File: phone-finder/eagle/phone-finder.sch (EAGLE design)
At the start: 45 parts, among them J1 MICRO USB, J2 PHONE-JACK, K1 RELAY, Q1 12Mhz, Q2 2N2222, Q3 2N2222, T1 DTA114EET1G (2x10K), U1 AP2114H-3.3TRG1, U2 NUF2042XV6T1G, U3 LPC11U35FHI33/501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

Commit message: Layout work in progress.
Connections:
- removed net N$20: K12.S2, R12.2
- new net N$15: K12.S1, R12.2
- net N$11: now also K12.S2; no longer K12.S1
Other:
- moved on the sheet: U1
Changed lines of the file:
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@@
 <attribute name="PART" x="355.981" y="70.358" size="1.778" layer="95"/>
 </instance>
-<instance part="K1" gate="2" x="360.68" y="119.38" smashed="yes" rot="R270">
-<attribute name="PART" x="362.839" y="114.935" size="1.778" layer="95"/>
+<instance part="K1" gate="2" x="360.68" y="119.38" smashed="yes" rot="MR270">
+<attribute name="PART" x="358.521" y="114.935" size="1.778" layer="95" rot="MR0"/>
 </instance>
 <instance part="+5V3" gate="G$1" x="350.52" y="83.82" rot="MR0"/>
@@
 </segment>
 </net>
-<net name="N$20" class="0">
-<segment>
-<pinref part="R12" gate="G$1" pin="2"/>
-<pinref part="K1" gate="2" pin="S2"/>
-<wire x1="350.52" y1="119.38" x2="353.06" y2="119.38" width="0.1524" layer="91"/>
-</segment>
-</net>
 <net name="N$17" class="0">
 <segment>
@@
 <net name="N$11" class="0">
 <segment>
-<pinref part="K1" gate="2" pin="S1"/>
-<wire x1="368.3" y1="119.38" x2="370.84" y2="119.38" width="0.1524" layer="91"/>
 <wire x1="370.84" y1="119.38" x2="370.84" y2="114.3" width="0.1524" layer="91"/>
 <pinref part="J2" gate="G$1" pin="4"/>
 <wire x1="370.84" y1="114.3" x2="375.92" y2="114.3" width="0.1524" layer="91"/>
+<pinref part="K1" gate="2" pin="S2"/>
+<wire x1="368.3" y1="119.38" x2="370.84" y2="119.38" width="0.1524" layer="91"/>
 </segment>
 </net>
@@
 </segment>
 </net>
+<net name="N$15" class="0">
+<segment>
+<pinref part="R12" gate="G$1" pin="2"/>
+<pinref part="K1" gate="2" pin="S1"/>
+<wire x1="350.52" y1="119.38" x2="353.06" y2="119.38" width="0.1524" layer="91"/>
+</segment>
+</net>

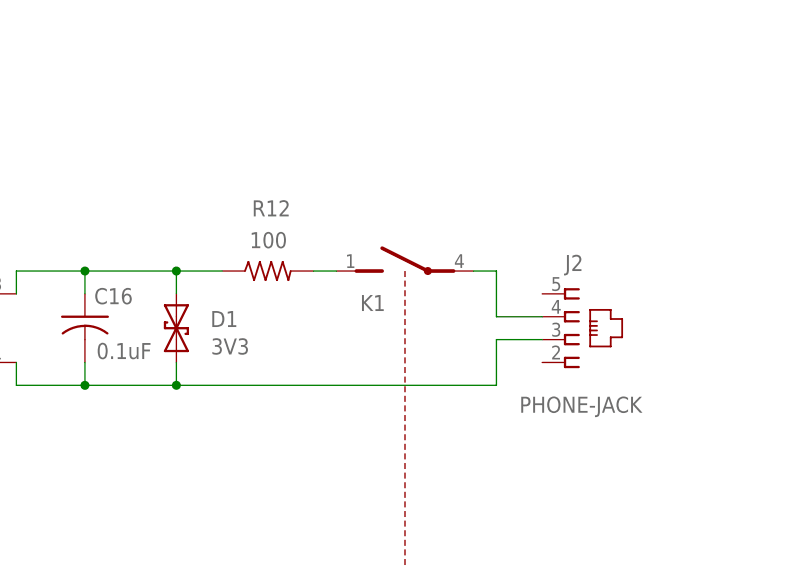
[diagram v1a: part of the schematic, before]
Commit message: Critical net routing done.
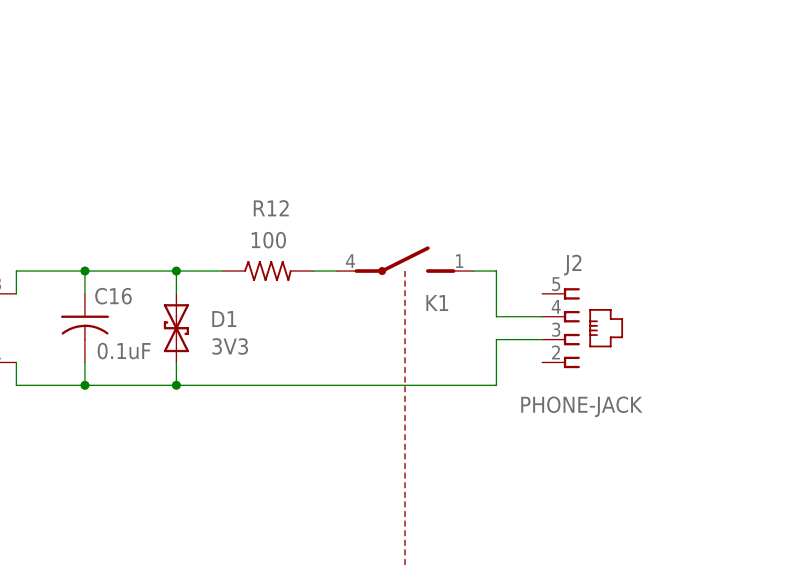
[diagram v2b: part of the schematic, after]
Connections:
- net N$11: now also K12.S1; no longer K12.S2
- net N$15: now also K12.S2; no longer K12.S1
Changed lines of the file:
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@@
 <attribute name="PART" x="355.981" y="70.358" size="1.778" layer="95"/>
 </instance>
-<instance part="K1" gate="2" x="360.68" y="119.38" smashed="yes" rot="MR270">
-<attribute name="PART" x="358.521" y="114.935" size="1.778" layer="95" rot="MR0"/>
+<instance part="K1" gate="2" x="360.68" y="119.38" smashed="yes" rot="R270">
+<attribute name="PART" x="362.839" y="114.935" size="1.778" layer="95"/>
 </instance>
 <instance part="+5V3" gate="G$1" x="350.52" y="83.82" rot="MR0"/>
@@
 <pinref part="J2" gate="G$1" pin="4"/>
 <wire x1="370.84" y1="114.3" x2="375.92" y2="114.3" width="0.1524" layer="91"/>
-<pinref part="K1" gate="2" pin="S2"/>
+<pinref part="K1" gate="2" pin="S1"/>
 <wire x1="368.3" y1="119.38" x2="370.84" y2="119.38" width="0.1524" layer="91"/>
 </segment>
@@
 <segment>
 <pinref part="R12" gate="G$1" pin="2"/>
-<pinref part="K1" gate="2" pin="S1"/>
+<pinref part="K1" gate="2" pin="S2"/>
 <wire x1="350.52" y1="119.38" x2="353.06" y2="119.38" width="0.1524" layer="91"/>
 </segment>

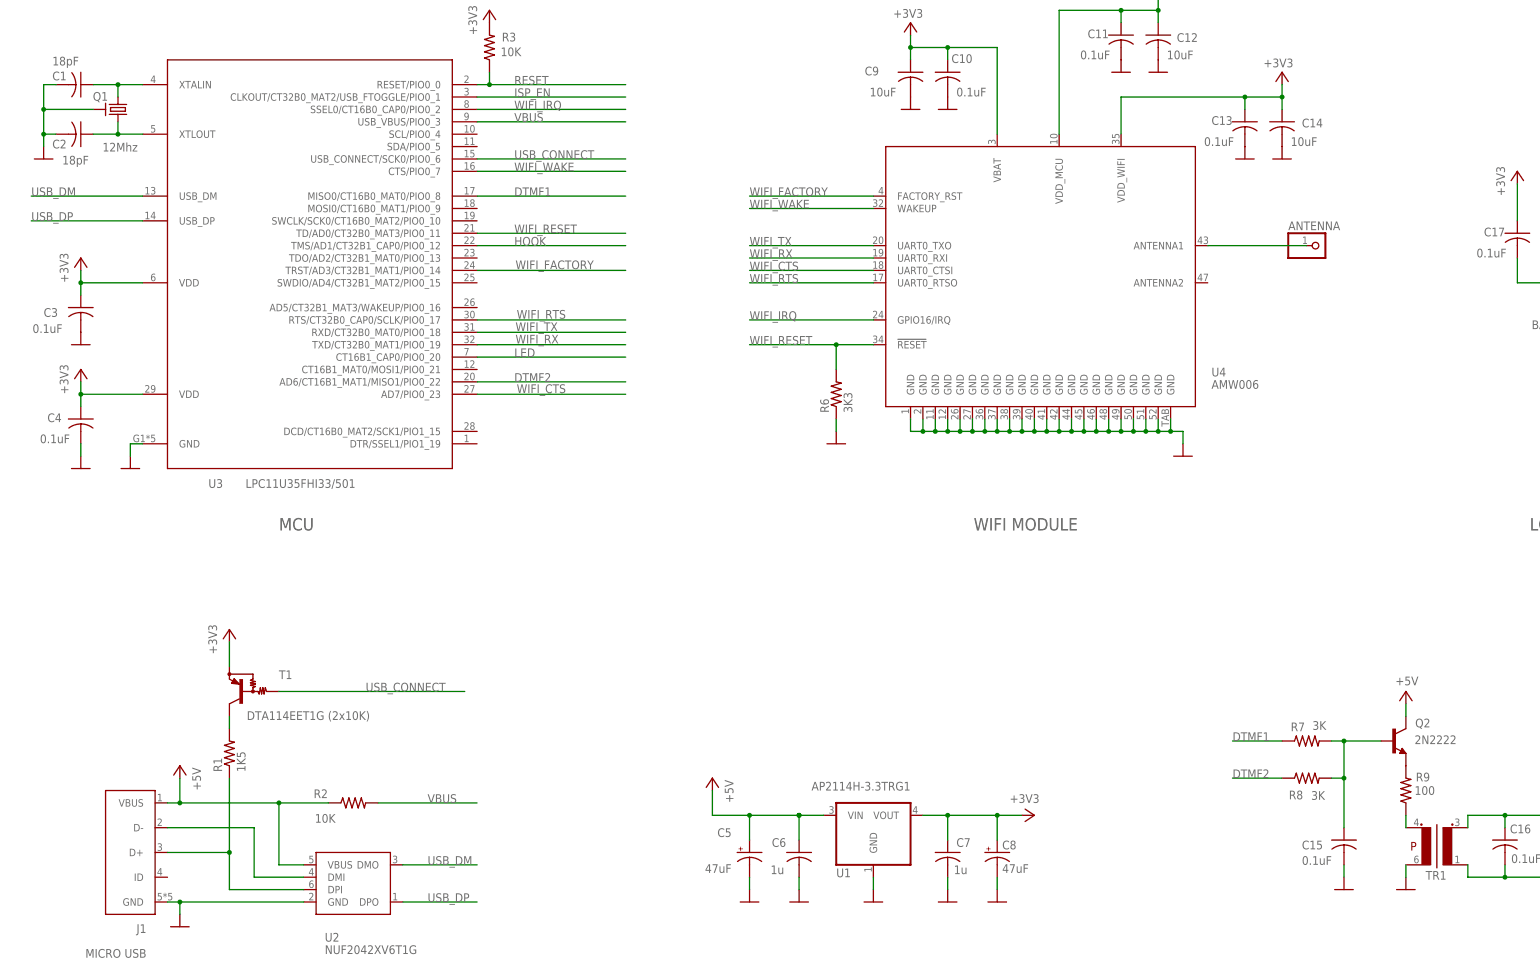
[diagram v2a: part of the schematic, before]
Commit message: Cleaned up component references.
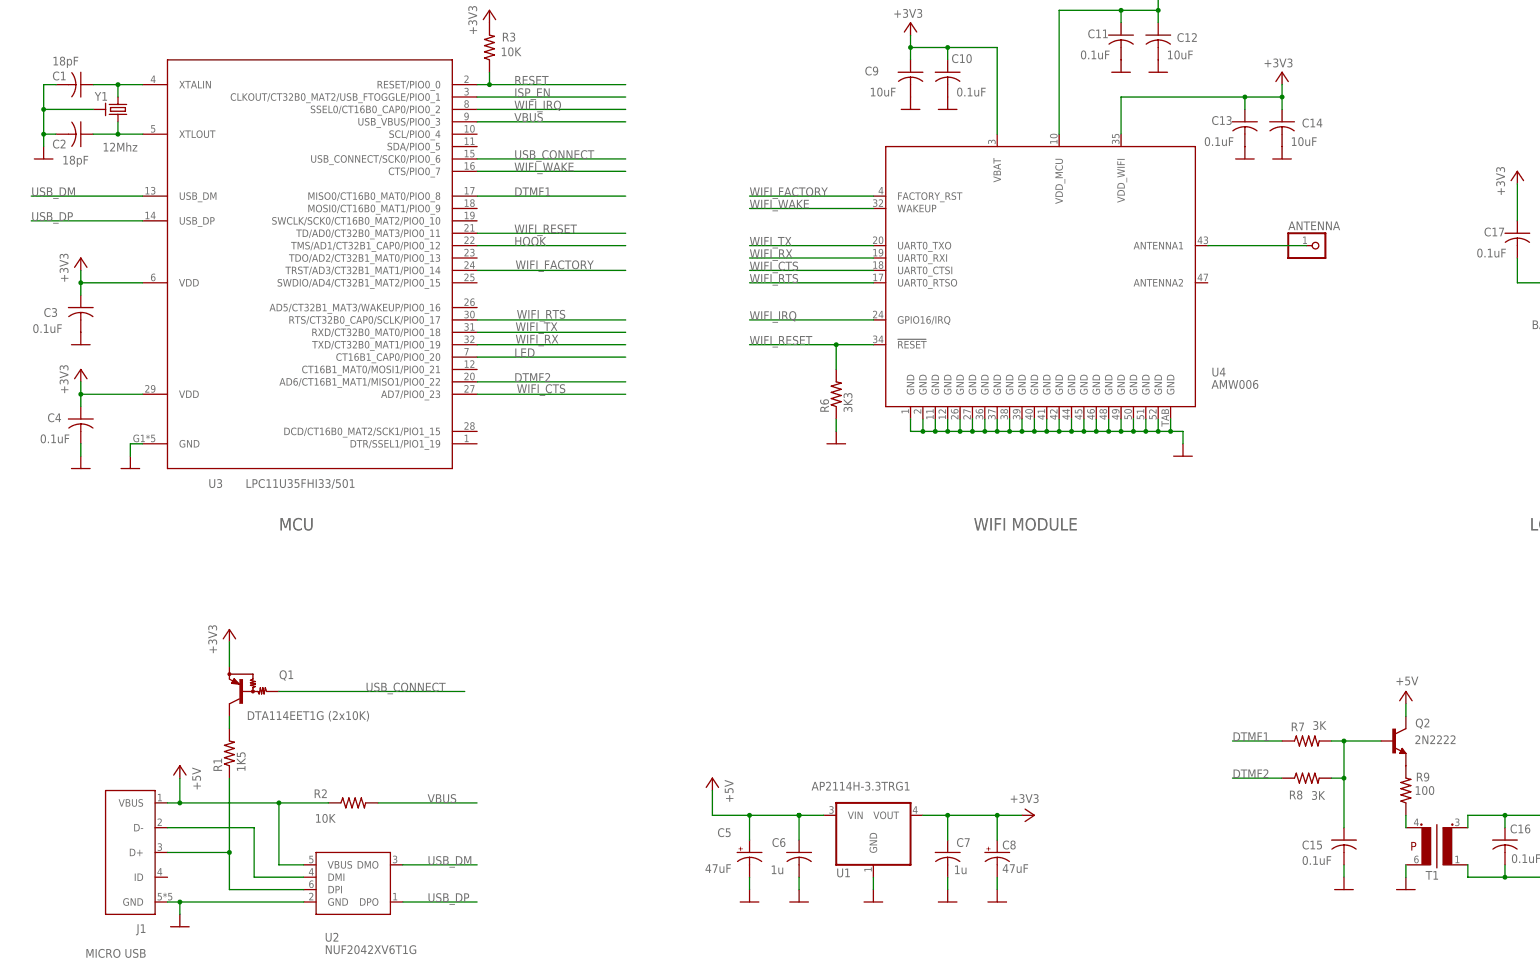
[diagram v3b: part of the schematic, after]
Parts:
- removed TR1: TRANSFORMER, phone-finder:TRANSFORMER
- added Y1: 12Mhz, phone-finder:CRYSTALCTS406
- Q1: value 12Mhz -> DTA114EET1G (2x10K); device phone-finder:CRYSTALCTS406 -> phone-finder:PNP-BIASED
- T1: value DTA114EET1G (2x10K) -> TRANSFORMER; device phone-finder:PNP-BIASED -> phone-finder:TRANSFORMER
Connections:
- net +3V3: now also Q1.E; no longer T1.E
- net GND: now also T1.P2, Y1.GND; no longer Q1.GND, TR1.P2
- net N$1: now also Y1.2; no longer Q1.2
- net N$10: now also T1.S2; no longer TR1.S2
- net N$17: now also T1.P1; no longer TR1.P1
- net N$3: now also Y1.1; no longer Q1.1
- net N$5: now also Q1.C; no longer T1.C
- net N$9: now also T1.S1; no longer TR1.S1
- net USB_CONNECT: now also Q1.B; no longer T1.B
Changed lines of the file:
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@@
 <part name="U3" library="phone-finder" deviceset="LPC11U35FHN33/501" device="" value="LPC11U35FHI33/501"/>
 <part name="GND2" library="phone-finder" deviceset="GND" device=""/>
-<part name="Q1" library="phone-finder" deviceset="CRYSTAL" device="CTS406" value="12Mhz"/>
+<part name="Y1" library="phone-finder" deviceset="CRYSTAL" device="CTS406" value="12Mhz"/>
 <part name="C1" library="phone-finder" deviceset="C" device="C0402K" value="18pF"/>
 <part name="C2" library="phone-finder" deviceset="C" device="C0402K" value="18pF"/>
@@
 <part name="R2" library="phone-finder" deviceset="R" device="R0402" value="10K"/>
 <part name="+3V9" library="phone-finder" deviceset="+3V3" device=""/>
-<part name="T1" library="phone-finder" deviceset="PNP-BIASED" device="" value="DTA114EET1G (2x10K)"/>
+<part name="Q1" library="phone-finder" deviceset="PNP-BIASED" device="" value="DTA114EET1G (2x10K)"/>
 <part name="U1" library="phone-finder" deviceset="LDO" device="SOT223" value="AP2114H-3.3TRG1"/>
 <part name="U2" library="phone-finder" deviceset="USB-ESD" device="" value="NUF2042XV6T1G"/>
@@
 <part name="+5V3" library="phone-finder" deviceset="+5V" device=""/>
 <part name="R11" library="phone-finder" deviceset="R" device="R0402" value="3K"/>
-<part name="TR1" library="phone-finder" deviceset="TRANSFORMER" device=""/>
+<part name="T1" library="phone-finder" deviceset="TRANSFORMER" device=""/>
 <part name="GND9" library="phone-finder" deviceset="GND" device=""/>
 <part name="D1" library="phone-finder" deviceset="DUAL-ZENER" device="" value="3V3"/>
@@
 </instance>
 <instance part="GND2" gate="1" x="43.18" y="190.5"/>
-<instance part="Q1" gate="G$1" x="40.64" y="264.16" smashed="yes" rot="R90">
+<instance part="Y1" gate="G$1" x="40.64" y="264.16" smashed="yes" rot="R90">
 <attribute name="NAME" x="38.608" y="267.716" size="1.778" layer="95" rot="R180"/>
 <attribute name="VALUE" x="44.704" y="257.302" size="1.778" layer="96" rot="R180"/>
@@
 </instance>
 <instance part="+3V9" gate="G$1" x="63.5" y="157.48"/>
-<instance part="T1" gate="G$1" x="66.04" y="144.78" smashed="yes" rot="MR0">
+<instance part="Q1" gate="G$1" x="66.04" y="144.78" smashed="yes" rot="MR0">
 <attribute name="NAME" x="73.66" y="147.32" size="1.778" layer="95"/>
 <attribute name="VALUE" x="67.056" y="138.938" size="1.778" layer="96"/>
@@
 <attribute name="VALUE" x="336.55" y="56.896" size="1.778" layer="96"/>
 </instance>
-<instance part="TR1" gate="G$1" x="309.88" y="111.76" smashed="yes">
+<instance part="T1" gate="G$1" x="309.88" y="111.76" smashed="yes">
 <attribute name="NAME" x="308.864" y="106.172" size="1.778" layer="95"/>
 </instance>
@@
 <wire x1="27.94" y1="259.08" x2="25.4" y2="259.08" width="0.1524" layer="91"/>
 <junction x="25.4" y="259.08"/>
-<pinref part="Q1" gate="G$1" pin="GND"/>
+<pinref part="Y1" gate="G$1" pin="GND"/>
 <wire x1="35.56" y1="264.16" x2="25.4" y2="264.16" width="0.1524" layer="91"/>
 <junction x="25.4" y="264.16"/>
@@
 <pinref part="GND9" gate="1" pin="GND"/>
 <wire x1="304.8" y1="106.68" x2="304.8" y2="109.22" width="0.1524" layer="91"/>
-<pinref part="TR1" gate="G$1" pin="P2"/>
+<pinref part="T1" gate="G$1" pin="P2"/>
 </segment>
 <segment>
@@
 <pinref part="U3" gate="G$1" pin="XTALIN"/>
 <wire x1="35.56" y1="269.24" x2="40.64" y2="269.24" width="0.1524" layer="91"/>
-<pinref part="Q1" gate="G$1" pin="2"/>
+<pinref part="Y1" gate="G$1" pin="2"/>
 <wire x1="40.64" y1="269.24" x2="45.72" y2="269.24" width="0.1524" layer="91"/>
 <wire x1="40.64" y1="266.7" x2="40.64" y2="269.24" width="0.1524" layer="91"/>
@@
 <pinref part="U3" gate="G$1" pin="XTLOUT"/>
 <wire x1="35.56" y1="259.08" x2="40.64" y2="259.08" width="0.1524" layer="91"/>
-<pinref part="Q1" gate="G$1" pin="1"/>
+<pinref part="Y1" gate="G$1" pin="1"/>
 <wire x1="40.64" y1="259.08" x2="45.72" y2="259.08" width="0.1524" layer="91"/>
 <wire x1="40.64" y1="261.62" x2="40.64" y2="259.08" width="0.1524" layer="91"/>
@@
 <segment>
 <pinref part="+3V9" gate="G$1" pin="+3V3"/>
-<pinref part="T1" gate="G$1" pin="E"/>
+<pinref part="Q1" gate="G$1" pin="E"/>
 <wire x1="63.5" y1="154.94" x2="63.5" y2="149.86" width="0.1524" layer="91"/>
 </segment>
@@
 <label x="91.44" y="144.78" size="1.778" layer="95"/>
 <wire x1="73.66" y1="144.78" x2="111.76" y2="144.78" width="0.1524" layer="91"/>
-<pinref part="T1" gate="G$1" pin="B"/>
+<pinref part="Q1" gate="G$1" pin="B"/>
 </segment>
 </net>
@@
 <pinref part="R1" gate="G$1" pin="2"/>
 <wire x1="63.5" y1="139.7" x2="63.5" y2="137.16" width="0.1524" layer="91"/>
-<pinref part="T1" gate="G$1" pin="C"/>
+<pinref part="Q1" gate="G$1" pin="C"/>
 </segment>
 </net>
@@
 <net name="N$10" class="0">
 <segment>
-<pinref part="TR1" gate="G$1" pin="S2"/>
+<pinref part="T1" gate="G$1" pin="S2"/>
 <wire x1="317.5" y1="109.22" x2="317.5" y2="106.68" width="0.1524" layer="91"/>
 <wire x1="317.5" y1="106.68" x2="325.12" y2="106.68" width="0.1524" layer="91"/>
@@
 <segment>
 <pinref part="R9" gate="G$1" pin="1"/>
-<pinref part="TR1" gate="G$1" pin="P1"/>
+<pinref part="T1" gate="G$1" pin="P1"/>
 <wire x1="304.8" y1="119.38" x2="304.8" y2="116.84" width="0.1524" layer="91"/>
 </segment>
@@
 <segment>
 <wire x1="317.5" y1="119.38" x2="317.5" y2="116.84" width="0.1524" layer="91"/>
-<pinref part="TR1" gate="G$1" pin="S1"/>
+<pinref part="T1" gate="G$1" pin="S1"/>
 <wire x1="317.5" y1="119.38" x2="325.12" y2="119.38" width="0.1524" layer="91"/>
 <pinref part="C16" gate="G$1" pin="1"/>

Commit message: Added board label.
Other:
- note added: "1.0"
- note removed: "0"
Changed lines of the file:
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@@
 <wire x1="406.4" y1="0" x2="0" y2="0" width="0.1524" layer="94"/>
 <wire x1="0" y1="0" x2="0" y2="304.8" width="0.1524" layer="94"/>
-<text x="400.812" y="7.874" size="2.54" layer="97">0</text>
+<text x="395.732" y="7.874" size="2.54" layer="97">1.0</text>
 <text x="68.58" y="81.28" size="2.54" layer="97">USB</text>
 <text x="73.66" y="177.8" size="2.54" layer="97">MCU</text>

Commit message: Performed final auto routing.
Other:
- moved on the sheet: D3, R13
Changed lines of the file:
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@@
 <wire x1="360.68" y1="73.66" x2="355.6" y2="73.66" width="0.1524" layer="94" style="shortdash"/>
 <text x="287.02" y="81.28" size="2.54" layer="97">PHONE LINE INTERFACE</text>
-<text x="187.96" y="12.7" size="2.54" layer="97">LED</text>
+<text x="190.5" y="17.78" size="2.54" layer="97">LED</text>
 </plain>
 <instances>
@@
 <attribute name="VALUE" x="373.38" y="103.632" size="1.778" layer="96"/>
 </instance>
-<instance part="D3" gate="1" x="203.2" y="35.56"/>
-<instance part="GND10" gate="1" x="203.2" y="25.4"/>
-<instance part="R13" gate="G$1" x="195.58" y="45.72" smashed="yes">
-<attribute name="NAME" x="194.564" y="47.7266" size="1.778" layer="95"/>
-<attribute name="VALUE" x="188.468" y="47.498" size="1.778" layer="96"/>
+<instance part="D3" gate="1" x="208.28" y="35.56"/>
+<instance part="GND10" gate="1" x="208.28" y="25.4"/>
+<instance part="R13" gate="G$1" x="200.66" y="45.72" smashed="yes">
+<attribute name="NAME" x="199.644" y="47.7266" size="1.778" layer="95"/>
+<attribute name="VALUE" x="193.548" y="47.498" size="1.778" layer="96"/>
 </instance>
 </instances>
@@
 <pinref part="D3" gate="1" pin="C"/>
 <pinref part="GND10" gate="1" pin="GND"/>
-<wire x1="203.2" y1="30.48" x2="203.2" y2="27.94" width="0.1524" layer="91"/>
+<wire x1="208.28" y1="30.48" x2="208.28" y2="27.94" width="0.1524" layer="91"/>
 </segment>
 </net>
@@
 <segment>
 <pinref part="R13" gate="G$1" pin="1"/>
-<wire x1="190.5" y1="45.72" x2="180.34" y2="45.72" width="0.1524" layer="91"/>
-<label x="180.34" y="45.72" size="1.778" layer="95"/>
+<wire x1="195.58" y1="45.72" x2="185.42" y2="45.72" width="0.1524" layer="91"/>
+<label x="185.42" y="45.72" size="1.778" layer="95"/>
 </segment>
 </net>
@@
 <pinref part="R13" gate="G$1" pin="2"/>
 <pinref part="D3" gate="1" pin="A"/>
-<wire x1="200.66" y1="45.72" x2="203.2" y2="45.72" width="0.1524" layer="91"/>
-<wire x1="203.2" y1="45.72" x2="203.2" y2="38.1" width="0.1524" layer="91"/>
-</segment>
-</net>
+<wire x1="205.74" y1="45.72" x2="208.28" y2="45.72" width="0.1524" layer="91"/>
+<wire x1="208.28" y1="45.72" x2="208.28" y2="38.1" width="0.1524" layer="91"/>
+</segment>
+</net>
